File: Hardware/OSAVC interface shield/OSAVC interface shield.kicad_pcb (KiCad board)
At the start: 2 copper layers, 101.6 x 53.3 mm, 37 parts, among them J1 DIGITAL, J11 I2C1, J12 GPS, J13 Radio, J14 RC RX, J2 COMMUNICATION, J20 Left Motor, J21 Right Motor, J22 Steering, J23 Encoder 4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

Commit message: fixed errors in layout
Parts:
- moved J2 2.54 mm to (106.7, 40.6)
- moved J3 2.54 mm to (62.2, 43.2)
- moved J12 2.54 mm to (109.2, 48.3)
- moved J13 2.54 mm to (109.2, 54.6)
- moved J14 2.54 mm to (109.2, 61.0)
- moved J9 2.54 mm to (83.8, 43.2)
- moved D1 1.27 mm to (125.7, 54.6)
- moved D2 1.27 mm to (125.7, 48.3)
- moved D4 1.27 mm to (125.7, 61.0)
- moved R3 1.27 mm to (125.7, 52.1)
- moved R4 1.27 mm to (125.7, 45.7)
- moved R6 1.27 mm to (125.7, 58.4)
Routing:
- net /SDO1: track 21.7 -> 25.7 mm
- net /SDI1: track 17.2 -> 13.2 mm, vias 1 -> 0
- net /OC2: track 72.9 -> 76.4 mm
- net /RA4: track 66.4 -> 69.6 mm
- net /RA1: track 70.8 -> 73.9 mm
- net /RA0: track 75.1 -> 78.0 mm
- net /SCL2: track 27.7 -> 30.3 mm
- net /RA5: track 62.1 -> 64.6 mm
- net /SDA1: track 50.2 -> 52.8 mm
- net /OC5: track 53.5 -> 56.1 mm
- net /OC4: track 57.9 -> 60.4 mm
- net +5V: track 109.6 -> 112.1 mm
- net /SCL1: track 57.8 -> 60.3 mm
- net /SDA2: track 26.7 -> 29.2 mm
- net /RE9: track 42.9 -> 45.1 mm
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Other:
- board text added: "OSAVC I/O rev 1"

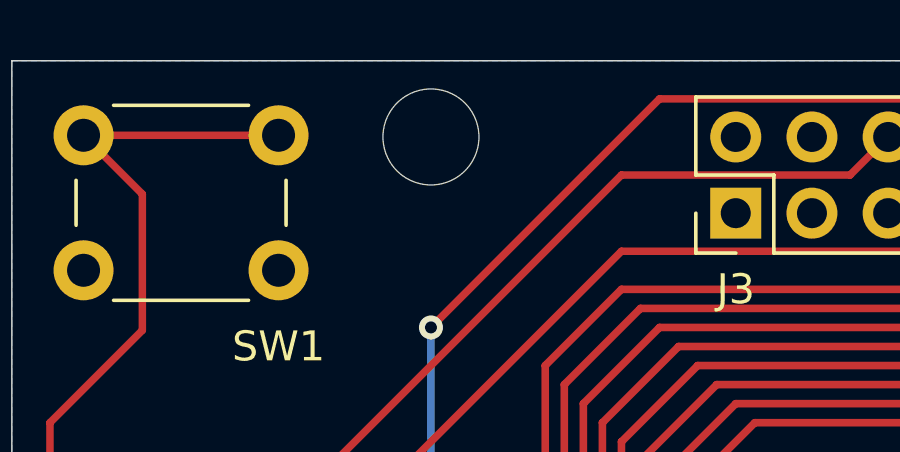
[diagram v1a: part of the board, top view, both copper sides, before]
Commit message: PCB fix, changed steering to left stick on passthrough mode
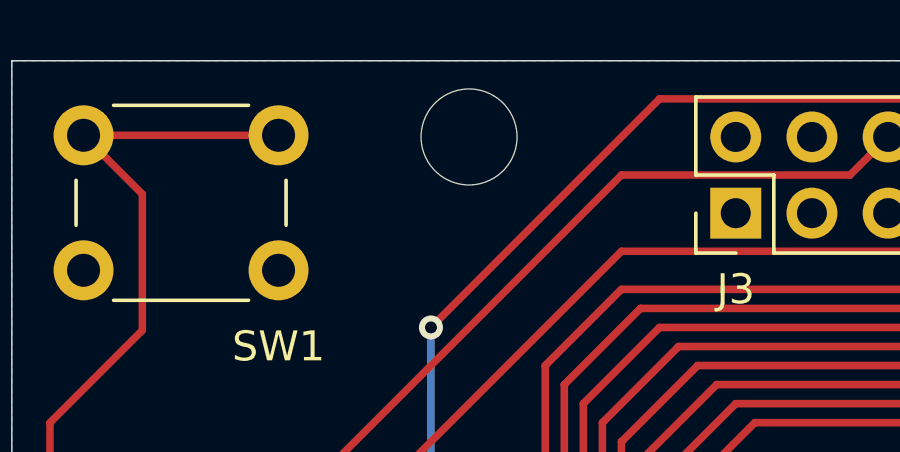
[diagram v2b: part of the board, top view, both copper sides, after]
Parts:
- moved REF** 1.27 mm to (53.3, 40.6)

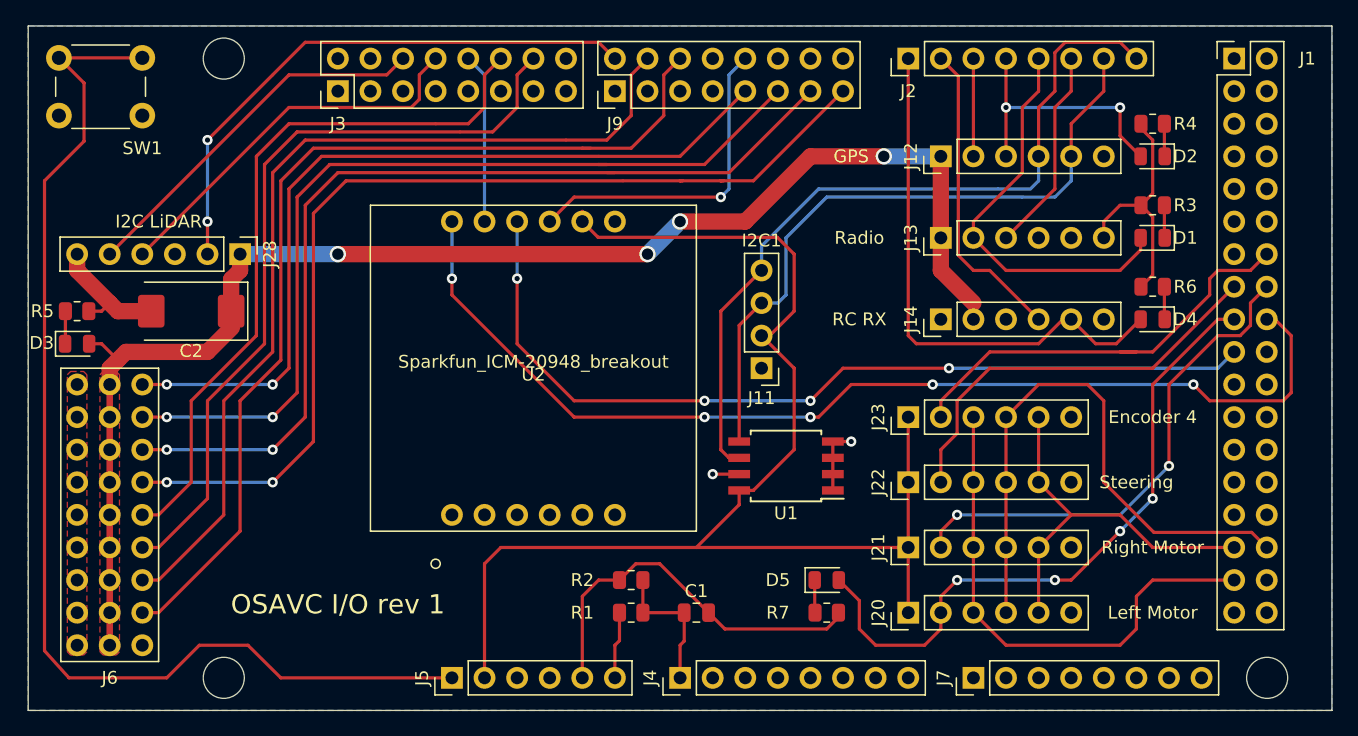
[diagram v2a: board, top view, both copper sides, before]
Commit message: IMU: added high resolution message; I/O board:  minor fixes and added pullup resistors
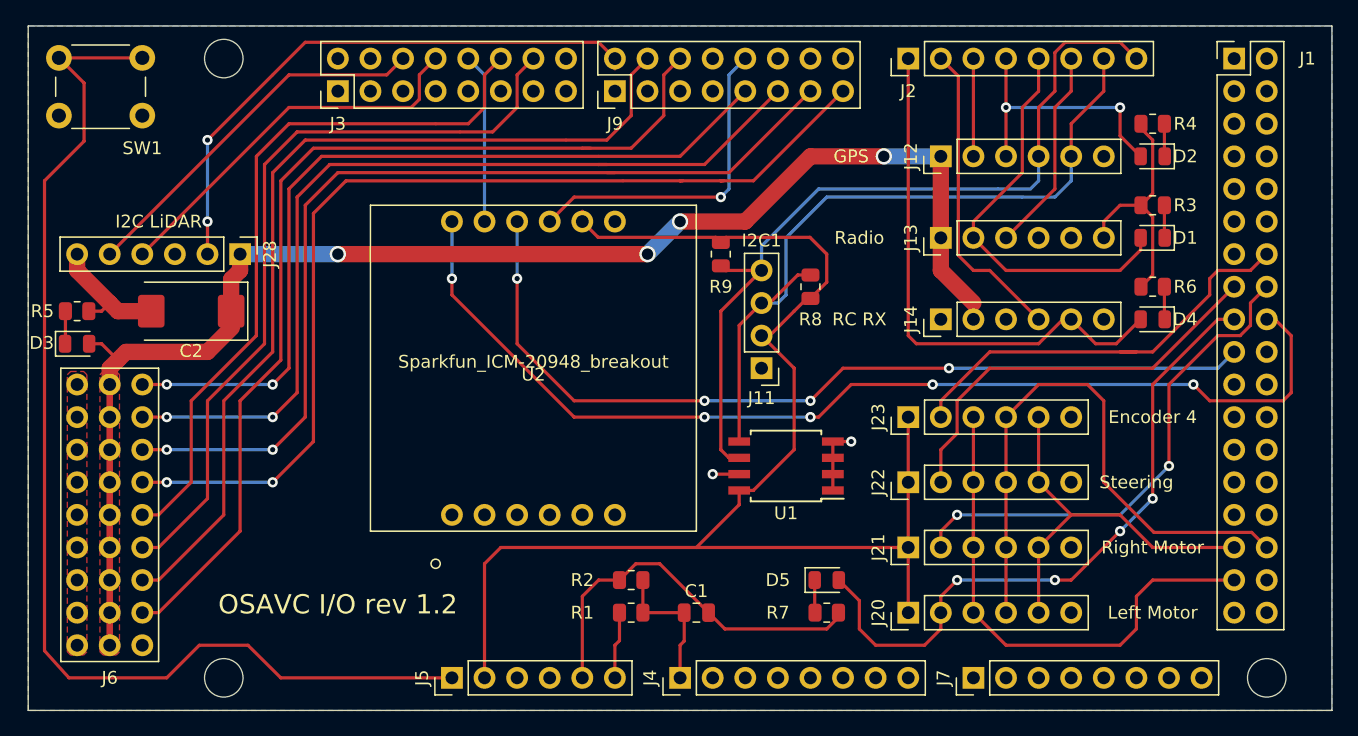
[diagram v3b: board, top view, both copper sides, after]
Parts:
- removed REF** (x3): MountingHole_3.2mm_M3, MountingHole:MountingHole_3.2mm_M3
- added H1: MountingHole, MountingHole:MountingHole_3mm, F.Cu at (53.3, 88.9)
- added H2: MountingHole, MountingHole:MountingHole_3mm, F.Cu at (53.3, 40.6)
- added H3: MountingHole, MountingHole:MountingHole_3mm, F.Cu at (134.6, 88.9)
- added R8: 4.7K, Resistor_SMD:R_0805_2012Metric, F.Cu at (99.1, 58.4)
- added R9: 4.7K, Resistor_SMD:R_0805_2012Metric, F.Cu at (92.1, 55.9)
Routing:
- net /SDA1: track 52.8 -> 57.5 mm
- net /SCL1: track 60.3 -> 63.6 mm
- net +3V3: track 105.2 -> 108.5 mm
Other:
- board text added: "OSAVC I/O rev 1.2"
- board text removed: "OSAVC I/O rev 1"
